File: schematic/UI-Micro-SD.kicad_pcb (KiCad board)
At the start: 2 copper layers, 86.4 x 51.4 mm, 31 parts, among them IC1 TCA9534PWR, J1 Conn_02x08_Odd_Even, J2 Conn_02x08_Odd_Even, J6 Conn_01x08, J8 Solder-Jumper-3-3-3-Open, Q1 BSS138, U1 SFV14R-2STE1HLF, U2 DizzyBITLogo, U3 DizzyBIT-Layout

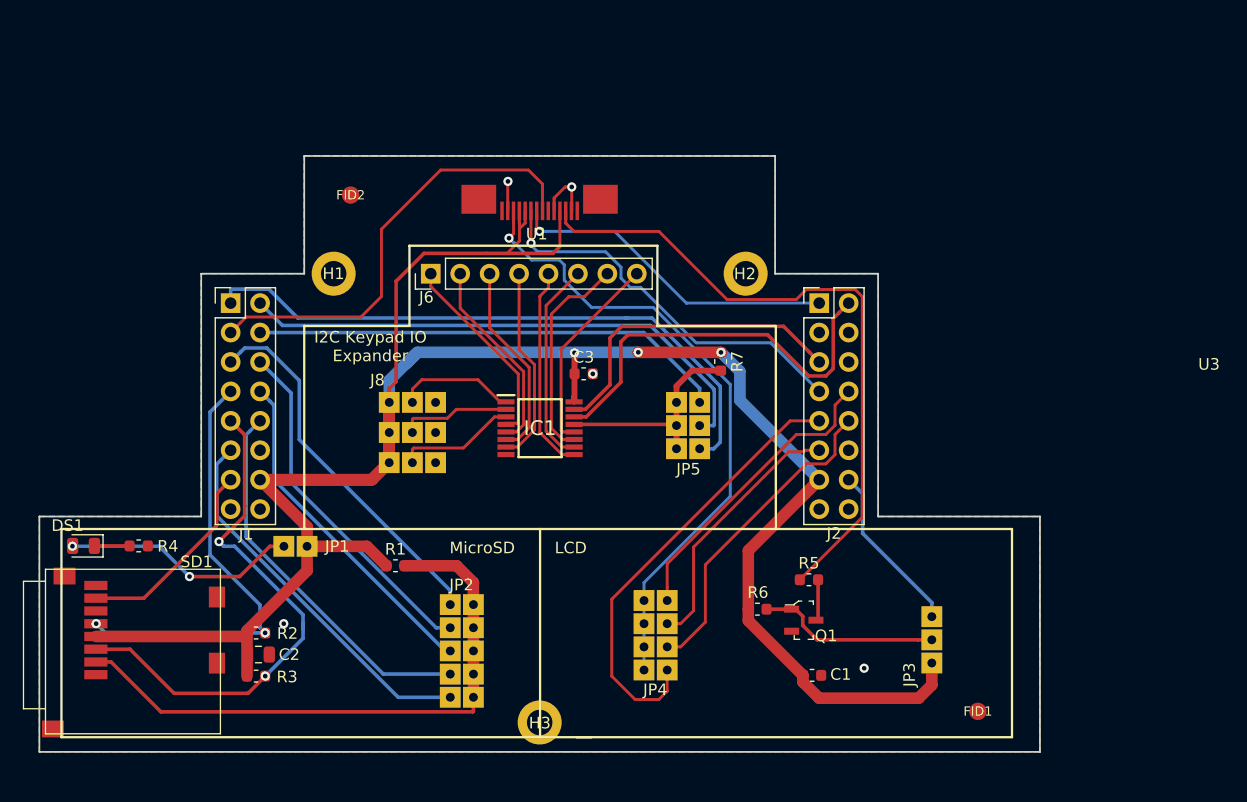
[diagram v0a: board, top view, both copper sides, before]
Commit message: Fixed PN-s for display connector and IO expander
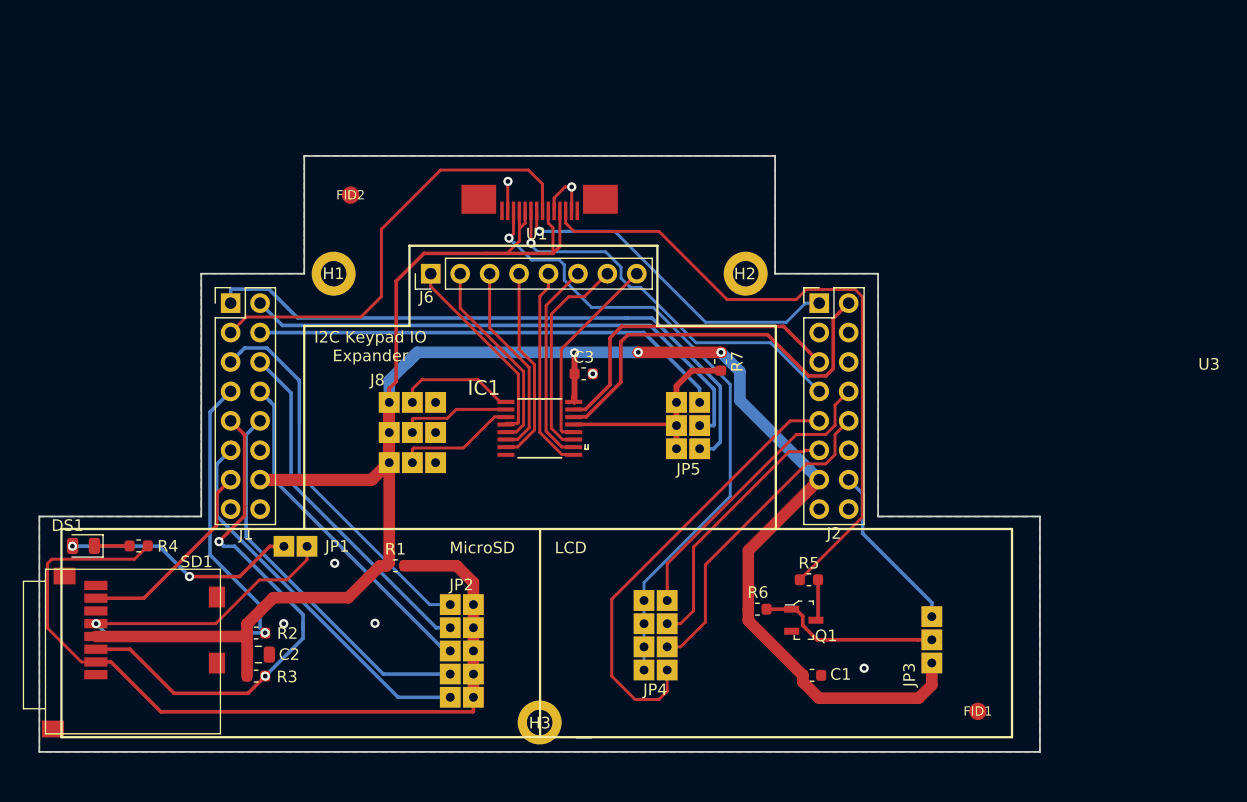
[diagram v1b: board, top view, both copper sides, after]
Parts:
- IC1: value TCA9534PWR -> TCA9554APWR; footprint undo:SOP65P640X120-16N -> SOP65P640X120-16N
- R5: value R -> 4R7 Ohm
- R6: value R -> R10K
- U1: value SFV14R-2STE1HLF -> SFV14R-3STBE1HLF; footprint undo:SFV14R-2STE1HLF -> undo:SFV14R-3STBE1HLF
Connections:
- JP1 pad 1: +3V3 -> HSPI_CLK
- R4 pad 2: GND -> HSPI_CS
- U1 pad 6: (no net) -> +3V3
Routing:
- net HSPI_CLK: track 38.5 -> 60.1 mm
- net HSPI_CS: track 52.0 -> 72.3 mm
- net VSPI_MOSI: track 28.6 -> 36.4 mm
- net +3V3: track 201.2 -> 204.4 mm
- net IO26: track 32.3 -> 33.4 mm
- net GND: vias 5 -> 7

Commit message: Major Update. Changed pin configuration and board outline.
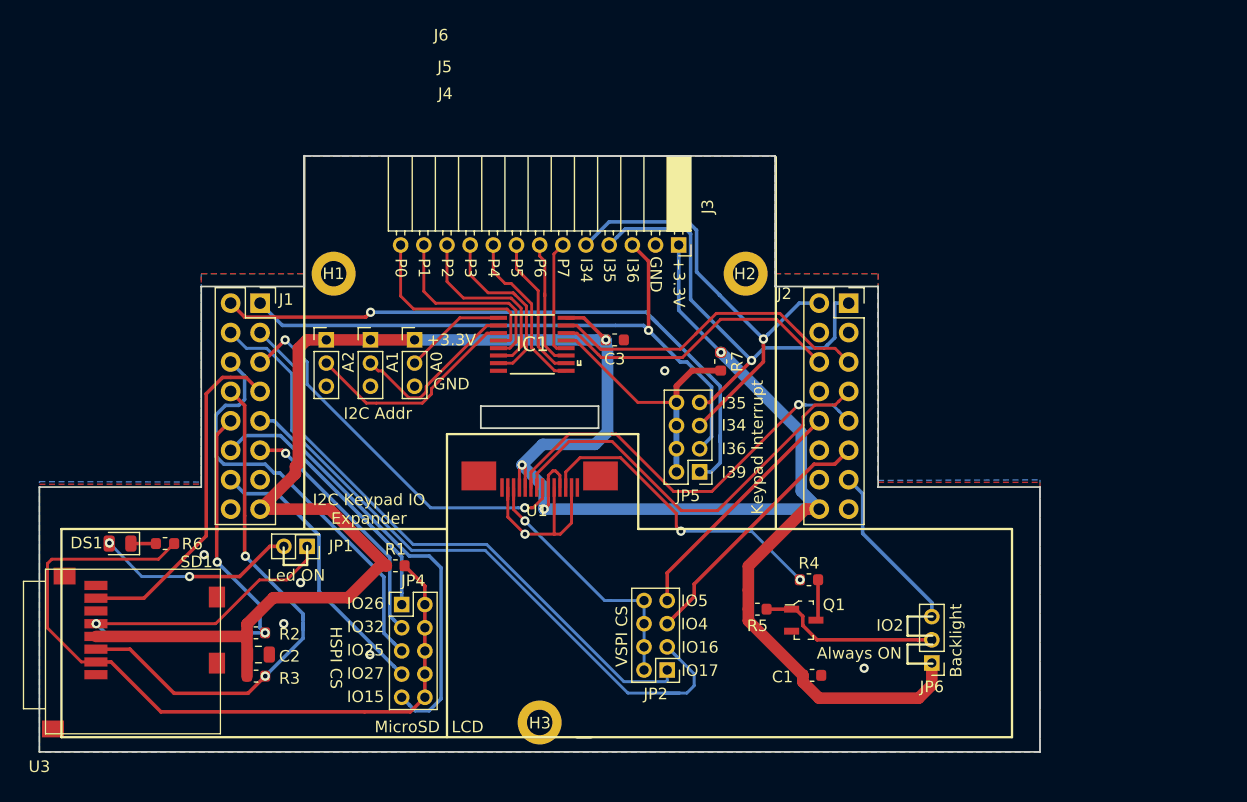
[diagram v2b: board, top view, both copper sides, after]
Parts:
- removed FID1, FID2: FIDUCIAL-1.5mm, fab:FIDUCIAL-1.5mm
- removed J8: Solder-Jumper-3-3-3-Open, DizzyBit:DizzyBit-SolderJumper-3-3-3-Open
- removed JP3: SolderJumper_3_Bridged12, DizzyBit:DizzyBit-SolderJumper-3-Open
- added J3: Conn_01x13, Connector_PinSocket_2.00mm:PinSocket_1x13_P2.00mm_Horizontal, F.Cu at (131.4, 102.3)
- added J4: Conn_01x03, Connector_PinHeader_2.00mm:PinHeader_1x03_P2.00mm_Vertical, F.Cu at (108.6, 110.5)
- added J5: Conn_01x03, Connector_PinHeader_2.00mm:PinHeader_1x03_P2.00mm_Vertical, F.Cu at (104.8, 110.5)
- added JP6: Conn_01x03, Connector_PinHeader_2.00mm:PinHeader_1x03_P2.00mm_Vertical, F.Cu at (153.2, 138.4)
- J1, J2: footprint Connector_PinHeader_2.54mm:PinHeader_2x08_P2.54mm_Vertical -> Connector_PinSocket_2.54mm:PinSocket_2x08_P2.54mm_Vertical
- J6: value Conn_01x08 -> Conn_01x03; footprint Connector_PinHeader_2.54mm:PinHeader_1x08_P2.54mm_Vertical -> Connector_PinHeader_2.00mm:PinHeader_1x03_P2.00mm_Vertical
- JP1: value SolderJumper_2_Bridged -> Conn_01x02; footprint DizzyBit:DizzyBit-SolderJumper-2-Open -> Connector_PinHeader_2.00mm:PinHeader_2x01_P2.00mm_Vertical
- JP2: value Conn_02x05_Odd_Even -> Conn_02x04_Odd_Even; footprint DizzyBit:DizzyBit-SolderJumper-5-5-Open -> Connector_PinHeader_2.00mm:PinHeader_2x04_P2.00mm_Vertical
- JP4: value Conn_02x04_Odd_Even -> Conn_02x05_Odd_Even; footprint DizzyBit:DizzyBit-SolderJumper-4-4-Open -> Connector_PinHeader_2.00mm:PinHeader_2x05_P2.00mm_Vertical
- JP5: value Conn_02x03_Odd_Even -> Conn_02x04_Odd_Even; footprint DizzyBit:DizzyBit-SolderJumper-3-3-Open -> Connector_PinHeader_2.00mm:PinHeader_2x04_P2.00mm_Vertical
- R4: value R330 -> 4R7 Ohm
- R5: value 4R7 Ohm -> R10K
- R6: value R10K -> R330
- moved U3 106.8 mm to (76.2, 146.1)
- moved R4 57.9 mm to (142.6, 131.2)
- moved R6 51.4 mm to (87.0, 128.1), turned to 0 degrees
- moved U2 30.0 mm to (143.3, 134.4)
- moved JP4 24.8 mm to (107.5, 133.3), turned to 0 degrees
- moved U1 23.9 mm to (119.1, 125.7)
- moved JP2 20.8 mm to (130.4, 139.0), turned to 180 degrees
- moved J6 10.7 mm to (101.0, 110.5), turned to 0 degrees
- moved IC1 7.28 mm to (118.7, 110.9)
- moved R5 5.12 mm to (138.2, 133.7), turned to 180 degrees
- moved C3 3.97 mm to (125.9, 110.5)
- moved DS1 3.16 mm to (83.2, 128.1)
- moved J2 2.54 mm to (146.1, 107.3)
- moved J1 2.54 mm to (95.2, 107.3)
- moved JP1 1.41 mm to (99.3, 128.3)
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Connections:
- J1 pad 1: I39 -> I36
- J1 pad 10: IO27 -> HSPI_CLK
- J1 pad 11: IO15 -> IO32
- J1 pad 12: (no net) -> IO26
- J1 pad 13: HSPI_MISO -> (no net)
- J1 pad 14: +3V3 -> IO27
- J1 pad 15: (no net) -> +3V3
- J1 pad 2: I36 -> I39
- J1 pad 3: IO33 -> IO17
- J1 pad 4: I34 -> IO16
- J1 pad 5: IO26 -> IO33
- J1 pad 6: IO32 -> IO25
- J1 pad 7: HSPI_CLK -> HSPI_MISO
- J1 pad 8: IO25 -> HSPI_MOSI
- J1 pad 9: HSPI_MOSI -> IO15
- J2 pad 1: VSPI_MOSI -> I35
- J2 pad 10: IO16 -> IO5
- J2 pad 13: +3V3 -> IO2
- J2 pad 14: IO2 -> (no net)
- J2 pad 16: (no net) -> +3V3
- J2 pad 2: I2C_SCL -> I34
- J2 pad 6: (no net) -> I2C_SCL
- J2 pad 7: VSPI_CLK -> VSPI_MOSI
- J2 pad 8: IO5 -> (no net)
- J2 pad 9: IO17 -> VSPI_CLK
- J6 pad 1: P0 -> +3V3
- J6 pad 2: P1 -> A2
- J6 pad 3: P2 -> GND
- JP2 pad 1: IO26 -> IO17
- JP2 pad 2: HSPI_CS -> VSPI_CS
- JP2 pad 3: IO32 -> IO16
- JP2 pad 4: HSPI_CS -> VSPI_CS
- JP2 pad 5: IO25 -> IO4
- JP2 pad 6: HSPI_CS -> VSPI_CS
- JP2 pad 7: IO27 -> IO5
- JP2 pad 8: HSPI_CS -> VSPI_CS
- JP4 pad 1: IO17 -> IO26
- JP4 pad 2: VSPI_CS -> HSPI_CS
- JP4 pad 3: IO16 -> IO32
- JP4 pad 4: VSPI_CS -> HSPI_CS
- JP4 pad 5: IO4 -> IO25
- JP4 pad 6: VSPI_CS -> HSPI_CS
- JP4 pad 7: IO5 -> IO27
- JP4 pad 8: VSPI_CS -> HSPI_CS
- R4 pad 1: Net-(DS1-Pad1) -> LCD_LEDK
- R4 pad 2: HSPI_CS -> Net-(Q1-Pad3)
- R5 pad 1: LCD_LEDK -> LCD_BACKLIGHT
- R5 pad 2: Net-(Q1-Pad3) -> +3V3
- R6 pad 1: LCD_BACKLIGHT -> Net-(DS1-Pad1)
- R6 pad 2: +3V3 -> HSPI_CS
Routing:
- net I35: track 0.00 -> 39.0 mm, vias 0 -> 1
- net IO16: track 27.7 -> 63.1 mm
- net VSPI_CS: track 56.4 -> 23.6 mm
- net LCD_LEDK: track 56.7 -> 27.1 mm, vias 0 -> 2
- net IO17: track 39.1 -> 51.9 mm
- net HSPI_MISO: track 17.5 -> 29.8 mm
- net GND: track 7.66 -> 18.3 mm
- net I2C_SCL: track 35.3 -> 25.6 mm
- net IO26: track 33.4 -> 23.8 mm
- net I36: track 46.6 -> 55.7 mm, vias 0 -> 1
- net IO32: track 30.4 -> 21.5 mm, vias 0 -> 1
- net A2: track 10.4 -> 19.1 mm
- net IO27: track 33.0 -> 24.6 mm
- net P7: track 17.4 -> 10.2 mm
- net P6: track 18.5 -> 11.3 mm
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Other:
- outline, holes or cut-outs redrawn
- board text added: "DizzyBit - MicroSD & UI Shield V 1.0.4"
- board text added: "I36"
- board text added: "P0"
- board text added: "P1"
- board text added: "P2"
- board text added: "P3"
- board text added: "P4"
- board text added: "P5"
- board text added: "P6"
- board text added: "P7"
